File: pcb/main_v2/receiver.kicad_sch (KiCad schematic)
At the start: 17 parts, among them IC401 HMC374, IC402 RMS-30+, J401 CONMHF1-SMD-T

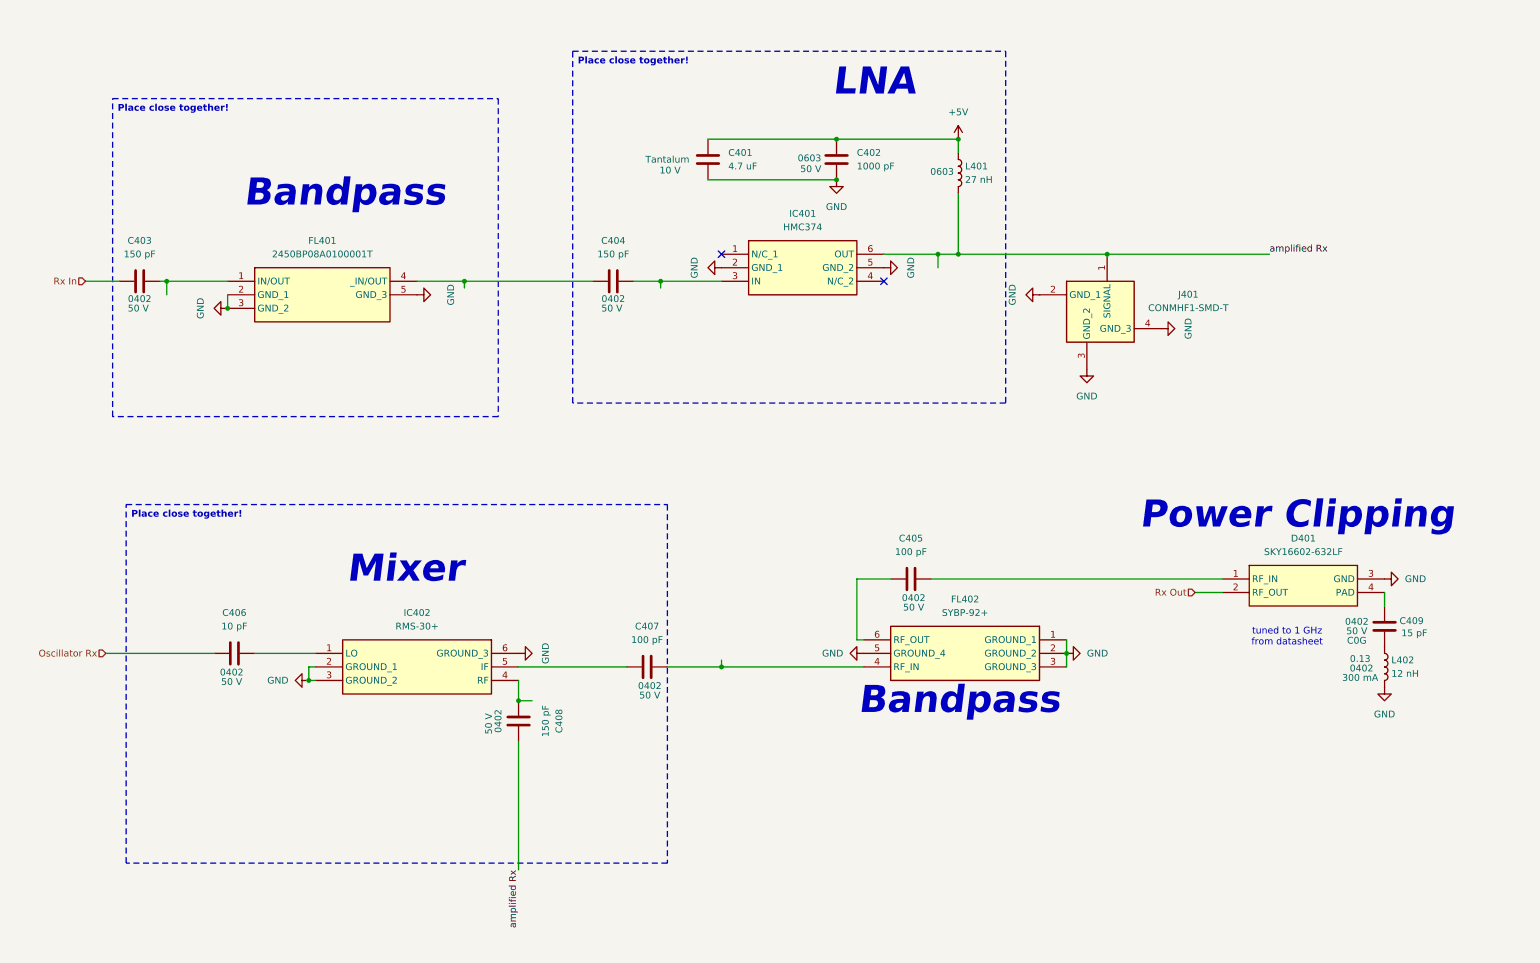
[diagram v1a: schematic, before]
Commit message: added second LNA
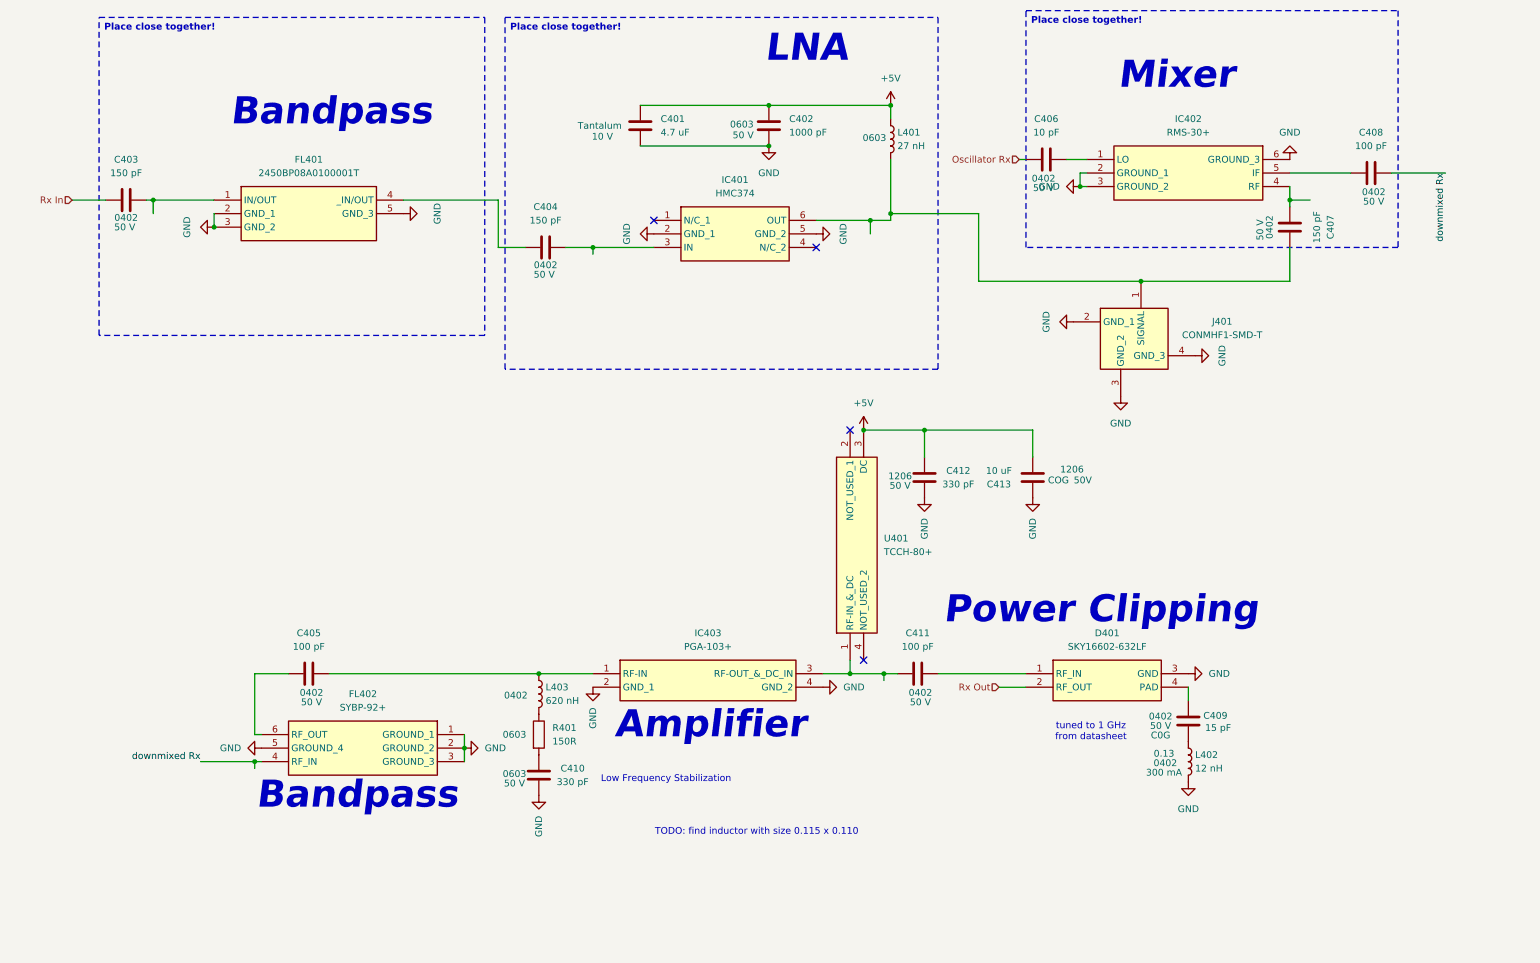
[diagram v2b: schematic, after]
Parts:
- added C410: 330 pF, Capacitor_SMD:C_0603_1608Metric, symbol Device:C
- added C411: 100 pF, Capacitor_SMD:C_0402_1005Metric, symbol Device:C
- added C412: 330 pF, Capacitor_SMD:C_1206_3216Metric, symbol Device:C
- added C413: 10 uF, Capacitor_SMD:C_1206_3216Metric, symbol Device:C
- added IC403: PGA-103+, My Footprints:GVA63, symbol My Symbols:PGA-103+
- added L403: 620 nH, Inductor_SMD:L_0402_1005Metric, symbol Device:L
- added R401: 150R, Resistor_SMD:R_0603_1608Metric, symbol Device:R
- added U401: TCCH-80+, My Footprints:TCCH80, symbol My Symbols:TCCH-80+
- C407: value 100 pF -> 150 pF
- C408: value 150 pF -> 100 pF
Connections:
- net +5V: now also C412.1, C413.1, U401.3 (DC)
- net GND: now also C410.2, C412.2, C413.2, IC403.2 (GND_1), IC403.4 (GND_2)
- net at IC402.4 (RF): now also C407.1; no longer C408.1
- net at D401.1 (RF_IN): now also C411.2; no longer C405.2
- net at IC402.5 (IF): now also C408.1; no longer C407.1
- net at C407.2: now also IC401.6 (OUT), J401.1 (SIGNAL), L401.2; no longer FL402.4 (RF_IN)
- removed net amplified Rx: C408.2, IC401.6 (OUT), J401.1 (SIGNAL), L401.2
- new net: C410.1, R401.2
- new net: C411.1, IC403.3 (RF-OUT_&_DC_IN), U401.1 (RF-IN_&_DC)
- new net: C405.2, IC403.1 (RF-IN), L403.1
- new net: L403.2, R401.1
- new net downmixed Rx: C408.2, FL402.4 (RF_IN)
- no-connect marks 2 -> 4
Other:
- note added: "Amplifier"
- note added: "Low Frequency Stabilization"
- note added: "TODO: find inductor with size 0.115 x 0.110"
- moved on the sheet: C401, C402, C403, C404, C405, C409, D401, FL401, FL402, IC401, J401, L401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

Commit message: added second LNA
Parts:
- removed L403: 620 nH, Inductor_SMD:L_0402_1005Metric, symbol Device:L
- added L404: LQW2UASR62F00L, LQW2UAS12NG00L, symbol My Symbols:LQW2UASR62F00L
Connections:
- net at C405.2, IC403.1 (RF-IN): now also L404.1
- net at R401.1: now also L404.2
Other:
- note removed: "TODO: find inductor with size 0.115 x 0.110"
- moved on the sheet: C410, R401

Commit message: updated project after assembly
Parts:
- L403: renamed from L404; value LQW2UASR62F00L -> 640 nH; footprint LQW2UAS12NG00L -> Inductor_SMD:L_0402_1005Metric; Height 2.03 -> (none); Manufacturer_Name Murata Electronics -> (none); Manufacturer_Part_Number LQW2UASR62F00L -> (none); Mouser Part Number 81-LQW2UASR62F00L -> (none); Mouser Price/Stock https://www.mouser.com/Search/Refine.aspx?Keyword=81-LQW2UA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 -> (none); Package (none) -> 0402
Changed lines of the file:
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@@
 		(in_pos_files yes)
 		(dnp no)
-		(property "Reference" "L404"
+		(property "Reference" "L403"
 			(at 114.3 151.1299 90)
 			(show_name no)
@@
 			)
 		)
-		(property "Value" "LQW2UASR62F00L"
+		(property "Value" "640 nH"
 			(at 114.3 153.6699 90)
 			(show_name no)
@@
 			)
 		)
-		(property "Footprint" "LQW2UAS12NG00L"
+		(property "Footprint" "Inductor_SMD:L_0402_1005Metric"
 			(at 15.57 158.75 0)
 			(hide yes)
@@
 			)
 		)
-		(property "Datasheet" "https://componentsearchengine.com/Datasheets/1/LQW2UASR62F00L.pdf"
+		(property "Datasheet" ""
 			(at -84.43 158.75 0)
 			(hide yes)
@@
 			)
 		)
-		(property "Description" "LQW2UAS_00 Series Inductor 620nH +/-1% 1008 (2520)"
+		(property "Description" ""
 			(at 111.76 142.24 0)
 			(hide yes)
@@
 			)
 		)
-		(property "Height" "2.03"
+		(property "Height" ""
 			(at -284.43 158.75 0)
 			(hide yes)
@@
 			)
 		)
-		(property "Mouser Part Number" "81-LQW2UASR62F00L"
+		(property "Mouser Part Number" ""
 			(at -384.43 158.75 0)
 			(hide yes)
@@
 			)
 		)
-		(property "Mouser Price/Stock" "https://www.mouser.com/Search/Refine.aspx?Keyword=81-LQW2UASR62F00L"
+		(property "Mouser Price/Stock" ""
 			(at -484.43 158.75 0)
 			(hide yes)
@@
 			)
 		)
-		(property "Manufacturer_Name" "Murata Electronics"
+		(property "Manufacturer_Name" ""
 			(at -584.43 158.75 0)
 			(hide yes)
@@
 			)
 		)
-		(property "Manufacturer_Part_Number" "LQW2UASR62F00L"
+		(property "Manufacturer_Part_Number" ""
 			(at -684.43 158.75 0)
 			(hide yes)
@@
 			)
 		)
+		(property "Package" "0402"
+			(at 111.76 142.24 90)
+			(hide yes)
+			(show_name no)
+			(do_not_autoplace no)
+			(effects
+				(font
+					(size 1.27 1.27)
+				)
+			)
+		)
 		(pin "1"
 		)
@@
 			(project "main_v2"
 				(path "/0599865e-4bed-44f1-b46e-4b55335b49b2/6cc491e9-db51-4c07-9c5c-0fdbb3f258a1"
-					(reference "L404")
+					(reference "L403")
 					(unit 1)
 				)

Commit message: updated assembly notes
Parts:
- L403: Inductanve 620 nH -> (none)
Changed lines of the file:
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@@
-			)
-		)
-		(property "Inductanve" "620 nH"
-			(at 106.934 152.146 90)
-			(show_name no)
-			(do_not_autoplace no)
-			(effects
-				(font
-					(size 1.27 1.27)
-				)
 			)
 		)
